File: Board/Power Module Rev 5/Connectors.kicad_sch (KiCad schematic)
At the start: 4 parts, among them J1 9-6437287-8, J3 Conn_01x16_Pin

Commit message: Board Progress
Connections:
- net 5V is gone; now on net GND: J1.11
- net CanHi is gone; now on net GND: J1.17
- net CanLo is gone; now on net GND: J1.16
- net GND: no longer J1.23, J1.24
- net Ignition: now also J1.3; no longer J1.22
- net L6699-IO1: now also J1.22; no longer J1.3
- net L6699-IO2: now also J1.23; no longer J1.4
- net L6699-IO3: now also J1.24; no longer J1.5
- net Sensor Gnd: no longer J1.10
- new net +5V: J1.10
- new net Can+: J1.4
- new net Can-: J1.5

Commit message: Update Board
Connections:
- net L6699-IO1 renamed Input1
- net L6699-IO2 renamed Input2
- net L6699-IO3 renamed Input3
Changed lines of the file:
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@@
     )
   )
-  (global_label "L6699-IO2" (shape input) (at 60.96 105.41 180) (fields_autoplaced)
+  (global_label "Input2" (shape input) (at 60.96 105.41 180) (fields_autoplaced)
     (effects (font (size 1.27 1.27)) (justify right))
-    (property "Intersheetrefs" "${INTERSHEET_REFS}" (at 47.4709 105.41 0)
+    (property "Intersheetrefs" "${INTERSHEET_REFS}" (at 52.0672 105.41 0)
       (effects (font (size 1.27 1.27)) (justify right) hide)
     )
@@
     )
   )
-  (global_label "L6699-IO3" (shape input) (at 60.96 107.95 180) (fields_autoplaced)
+  (global_label "Input3" (shape input) (at 60.96 107.95 180) (fields_autoplaced)
     (effects (font (size 1.27 1.27)) (justify right))
-    (property "Intersheetrefs" "${INTERSHEET_REFS}" (at 47.4709 107.95 0)
+    (property "Intersheetrefs" "${INTERSHEET_REFS}" (at 52.0672 107.95 0)
       (effects (font (size 1.27 1.27)) (justify right) hide)
     )
@@
     )
   )
-  (global_label "L6699-IO1" (shape input) (at 60.96 102.87 180) (fields_autoplaced)
+  (global_label "Input1" (shape input) (at 60.96 102.87 180) (fields_autoplaced)
     (effects (font (size 1.27 1.27)) (justify right))
-    (property "Intersheetrefs" "${INTERSHEET_REFS}" (at 47.4709 102.87 0)
+    (property "Intersheetrefs" "${INTERSHEET_REFS}" (at 52.0672 102.87 0)
       (effects (font (size 1.27 1.27)) (justify right) hide)
     )

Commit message: Update Board
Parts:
- C40: value C_Small -> 100nF; footprint (none) -> Capacitor_SMD:C_0603_1608Metric_Pad1.08x0.95mm_HandSolder
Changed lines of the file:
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@@
       (effects (font (size 1.27 1.27)) (justify left))
     )
-    (property "Value" "C_Small" (at 233.68 52.7113 0)
+    (property "Value" "100nF" (at 233.68 52.7113 0)
       (effects (font (size 1.27 1.27)) (justify left))
     )
-    (property "Footprint" "" (at 231.14 50.8 0)
+    (property "Footprint" "Capacitor_SMD:C_0603_1608Metric_Pad1.08x0.95mm_HandSolder" (at 231.14 50.8 0)
       (effects (font (size 1.27 1.27)) hide)
     )

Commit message: Board Update
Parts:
- J3: footprint Eagle_WP-BUCF (rev22a):WP-BUFU_7461147_HAL -> Eagle_WP-BUCF (rev22a):WP-BUFU_7461097_HAL
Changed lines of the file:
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@@
       (effects (font (size 1.27 1.27)))
     )
-    (property "Footprint" "Eagle_WP-BUCF (rev22a):WP-BUFU_7461147_HAL" (at 261.62 49.53 0)
+    (property "Footprint" "Eagle_WP-BUCF (rev22a):WP-BUFU_7461097_HAL" (at 261.62 49.53 0)
       (effects (font (size 1.27 1.27)) hide)
     )

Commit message: Board Update and Gerbers
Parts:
- C40: value 100nF -> 0.1uF
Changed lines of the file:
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@@
       (effects (font (size 1.27 1.27)) (justify left))
     )
-    (property "Value" "100nF" (at 233.68 52.7113 0)
+    (property "Value" "0.1uF" (at 233.68 52.7113 0)
       (effects (font (size 1.27 1.27)) (justify left))
     )

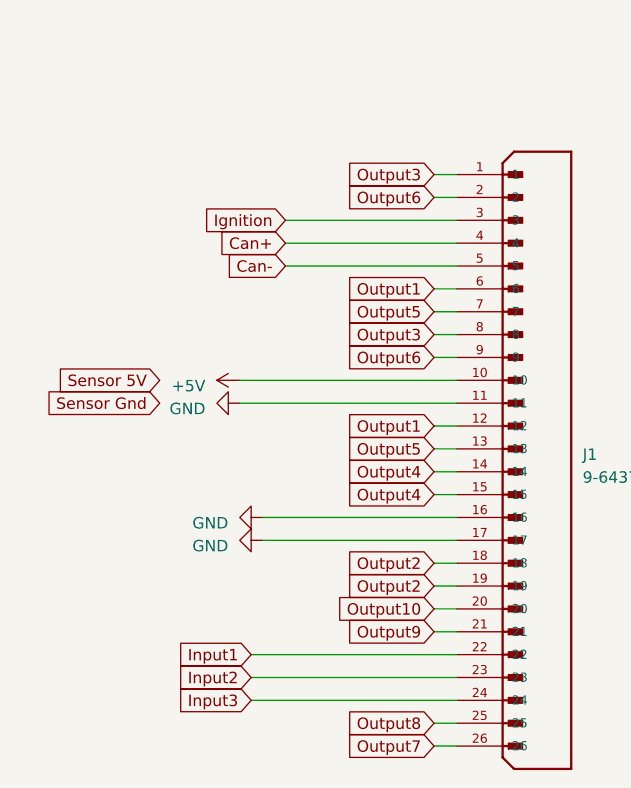
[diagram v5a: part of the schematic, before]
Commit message: Board - fixed connector pin numbering
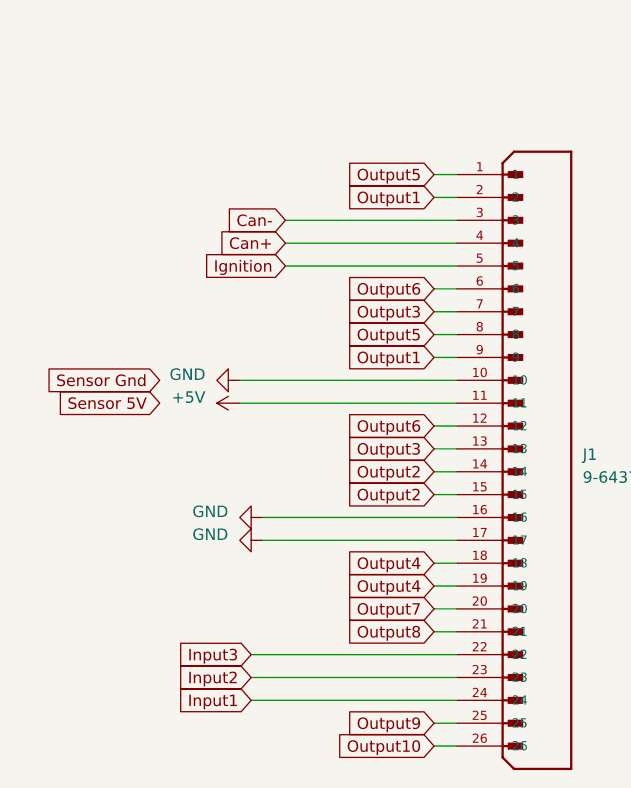
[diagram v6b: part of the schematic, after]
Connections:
- net +5V: now also J1.11; no longer J1.10
- net Can-: now also J1.3; no longer J1.5
- net GND: now also J1.10; no longer J1.11
- net Ignition: now also J1.5; no longer J1.3
- net Input1: now also J1.24; no longer J1.22
- net Input3: now also J1.22; no longer J1.24
- net Output1: now also J1.2, J1.9; no longer J1.12, J1.6
- net Output10: now also J1.26; no longer J1.20
- net Output2: now also J1.14, J1.15; no longer J1.18, J1.19
- net Output3: now also J1.13, J1.7; no longer J1.1, J1.8
- net Output4: now also J1.18, J1.19; no longer J1.14, J1.15
- net Output5: now also J1.1, J1.8; no longer J1.13, J1.7
- net Output6: now also J1.12, J1.6; no longer J1.2, J1.9
- net Output7: now also J1.20; no longer J1.26
- net Output8: now also J1.21; no longer J1.25
- net Output9: now also J1.25; no longer J1.21
